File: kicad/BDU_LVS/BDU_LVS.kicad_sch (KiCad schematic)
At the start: 31 parts, among them J1 Relay connector, J16 DCDC, J17 AMS, J2 Relay connector, J3 Relay connector, J4 Conn_01x02, K1 Relay_DPST-NO, K2 Relay_DPST-NO, K3 Relay_DPST-NO, U1 LTV-847S

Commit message: BDU_TS and LVS v1 done
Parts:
- J1, J17, J2, J3: footprint Connector_Molex:Molex_Micro-Fit_3.0_43650-0410_1x04-1MP_P3.00mm_Horizontal_PnP -> Connector_Molex:Molex_Micro-Fit_3.0_43650-0415_1x04_P3.00mm_Vertical
- J16, J4: footprint Connector_Molex:Molex_Micro-Fit_3.0_43650-0210_1x02-1MP_P3.00mm_Horizontal_PnP -> Connector_Molex:Molex_Micro-Fit_3.0_43650-0215_1x02_P3.00mm_Vertical
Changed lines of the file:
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@@
 			)
 		)
-		(property "Footprint" "Connector_Molex:Molex_Micro-Fit_3.0_43650-0410_1x04-1MP_P3.00mm_Horizontal_PnP"
+		(property "Footprint" "Connector_Molex:Molex_Micro-Fit_3.0_43650-0415_1x04_P3.00mm_Vertical"
 			(at 72.39 106.68 0)
 			(effects
@@
 			)
 		)
-		(property "Footprint" "Connector_Molex:Molex_Micro-Fit_3.0_43650-0210_1x02-1MP_P3.00mm_Horizontal_PnP"
+		(property "Footprint" "Connector_Molex:Molex_Micro-Fit_3.0_43650-0215_1x02_P3.00mm_Vertical"
 			(at 190.5 35.56 0)
 			(effects
@@
 			)
 		)
-		(property "Footprint" "Connector_Molex:Molex_Micro-Fit_3.0_43650-0410_1x04-1MP_P3.00mm_Horizontal_PnP"
+		(property "Footprint" "Connector_Molex:Molex_Micro-Fit_3.0_43650-0415_1x04_P3.00mm_Vertical"
 			(at 72.39 85.09 0)
 			(effects
@@
 			)
 		)
-		(property "Footprint" "Connector_Molex:Molex_Micro-Fit_3.0_43650-0410_1x04-1MP_P3.00mm_Horizontal_PnP"
+		(property "Footprint" "Connector_Molex:Molex_Micro-Fit_3.0_43650-0415_1x04_P3.00mm_Vertical"
 			(at 73.66 48.26 0)
 			(effects
@@
 			)
 		)
-		(property "Footprint" "Connector_Molex:Molex_Micro-Fit_3.0_43650-0410_1x04-1MP_P3.00mm_Horizontal_PnP"
+		(property "Footprint" "Connector_Molex:Molex_Micro-Fit_3.0_43650-0415_1x04_P3.00mm_Vertical"
 			(at 73.66 26.67 0)
 			(effects
@@
 			)
 		)
-		(property "Footprint" "Connector_Molex:Molex_Micro-Fit_3.0_43650-0210_1x02-1MP_P3.00mm_Horizontal_PnP"
+		(property "Footprint" "Connector_Molex:Molex_Micro-Fit_3.0_43650-0215_1x02_P3.00mm_Vertical"
 			(at 172.72 127 0)
 			(effects

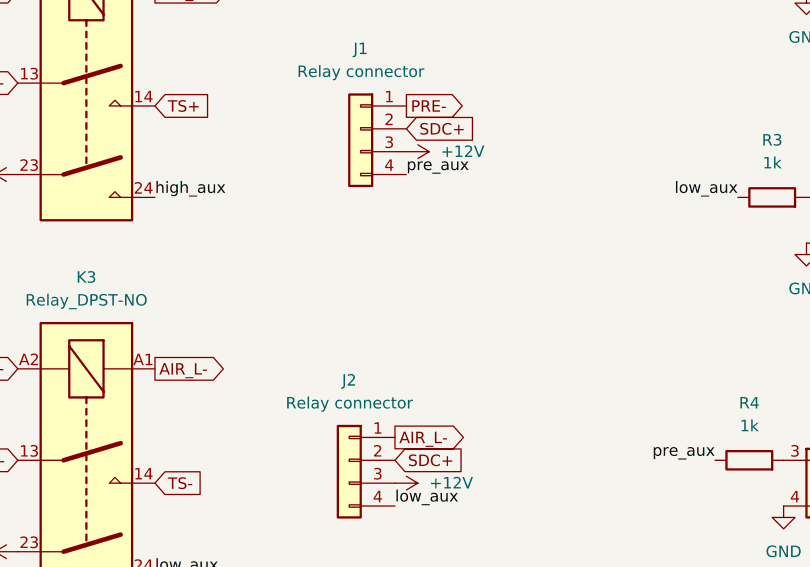
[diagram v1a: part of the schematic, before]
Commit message: BDU_LVS changes
Added connector for  TSAL-G of contactor Aux
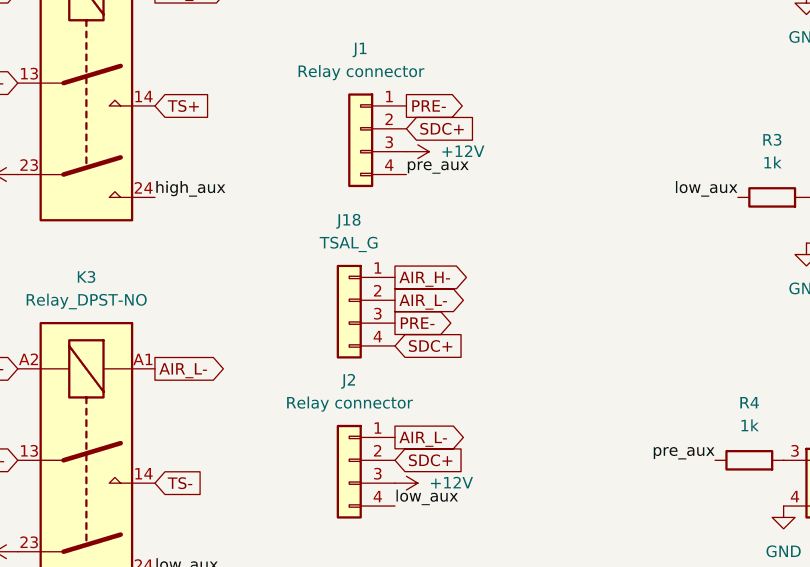
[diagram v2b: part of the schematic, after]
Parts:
- added J18: TSAL_G, Connector_Molex:Molex_Micro-Fit_3.0_43650-0415_1x04_P3.00mm_Vertical, symbol Connector_Generic:Conn_01x04
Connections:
- net AIR_H-: now also J18.1 (Pin_1)
- net AIR_L-: now also J18.2 (Pin_2)
- net PRE-: now also J18.3 (Pin_3)
- net SDC+: now also J18.4 (Pin_4)
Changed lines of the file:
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@@
+		)
+	)
+	(global_label "PRE-"
+		(shape output)
+		(at 77.47 69.85 0)
+		(fields_autoplaced yes)
+		(effects
+			(font
+				(size 1.27 1.27)
+			)
+			(justify left)
+		)
+		(property "Intersheetrefs" "${INTERSHEET_REFS}"
+			(at 85.7166 69.85 0)
+			(effects
+				(font
+					(size 1.27 1.27)
+				)
+				(justify left)
+				(hide yes)
+			)
 		)
 	)
@@
 	(global_label "SDC+"
 		(shape input)
-		(at 35.56 113.03 180)
+		(at 77.47 72.39 0)
 		(fields_autoplaced yes)
 		(effects
@@
 				(size 1.27 1.27)
 			)
+			(justify left)
+		)
+		(property "Intersheetrefs" "${INTERSHEET_REFS}"
+			(at 85.7771 72.39 0)
+			(effects
+				(font
+					(size 1.27 1.27)
+				)
+				(justify left)
+				(hide yes)
+			)
+		)
+	)
+	(global_label "SDC+"
+		(shape input)
+		(at 35.56 113.03 180)
+		(fields_autoplaced yes)
+		(effects
+			(font
+				(size 1.27 1.27)
+			)
 			(justify right)
 		)
@@
 		)
 	)
+	(global_label "AIR_H-"
+		(shape output)
+		(at 77.47 64.77 0)
+		(fields_autoplaced yes)
+		(effects
+			(font
+				(size 1.27 1.27)
+			)
+			(justify left)
+		)
+		(property "Intersheetrefs" "${INTERSHEET_REFS}"
+			(at 87.2891 64.77 0)
+			(effects
+				(font
+					(size 1.27 1.27)
+				)
+				(justify left)
+				(hide yes)
+			)
+		)
+	)
 	(global_label "BAT+"
 		(shape input)
@@
 		)
 	)
+	(global_label "AIR_L-"
+		(shape output)
+		(at 77.47 67.31 0)
+		(fields_autoplaced yes)
+		(effects
+			(font
+				(size 1.27 1.27)
+			)
+			(justify left)
+		)
+		(property "Intersheetrefs" "${INTERSHEET_REFS}"
+			(at 86.9867 67.31 0)
+			(effects
+				(font
+					(size 1.27 1.27)
+				)
+				(justify left)
+				(hide yes)
+			)
+		)
+	)
 	(global_label "BAT-"
 		(shape input)
@@
 					(unit 1)
 				)
+			)
+		)
+	)
+	(symbol
+		(lib_id "Connector_Generic:Conn_01x04")
+		(at 72.39 67.31 0)
+		(mirror y)
+		(unit 1)
+		(exclude_from_sim no)
+		(in_bom yes)
+		(on_board yes)
+		(dnp no)
+		(fields_autoplaced yes)
+		(property "Reference" "J18"
+			(at 72.39 58.42 0)
+			(effects
+				(font
+					(size 1.27 1.27)
+				)
+			)
+		)
+		(property "Value" "TSAL_G"
+			(at 72.39 60.96 0)
+			(effects
+				(font
+					(size 1.27 1.27)
+				)
+			)
+		)
+		(property "Footprint" "Connector_Molex:Molex_Micro-Fit_3.0_43650-0415_1x04_P3.00mm_Vertical"
+			(at 72.39 67.31 0)
+			(effects
+				(font
+					(size 1.27 1.27)
+				)
+				(hide yes)
+			)
+		)
+		(property "Datasheet" "~"
+			(at 72.39 67.31 0)
+			(effects
+				(font
+					(size 1.27 1.27)
+				)
+				(hide yes)
+			)
+		)
+		(property "Description" "Generic connector, single row, 01x04, script generated (kicad-library-utils/schlib/autogen/connector/)"
+			(at 72.39 67.31 0)
+			(effects
+				(font
+					(size 1.27 1.27)
+				)
+				(hide yes)
+			)
+		)
+		(pin "3"
+		)
+		(pin "1"
+		)
+		(pin "4"
+		)
+		(pin "2"
+		)
+		(instances
+			(project "BDU_LVS"
+				(path "/0b64c1d7-2532-4b12-a904-d5a6ad65971d"
+					(reference "J18")
+					(unit 1)
+				)
